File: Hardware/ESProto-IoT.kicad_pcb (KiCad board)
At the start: 2 copper layers, 68.6 x 53.3 mm, 55 parts, among them IC1 ARDUINO_PRO_MINI_5V, P1 DIGITAL_02, P10 DIGITAL_11, P11 DIGITAL_12, P12 DIGITAL_13X, P13 ANALOG_00, P14 ANALOG_01, P15 ANALOG_02, P16 ANALOG_03X, P17 I2C_01, P18 I2C_02, P19 I2C_03, P2 DIGITAL_03, P20 I2C_04, P21 POWER_L, P22 POWER_R, P23 ESP_G14, P24 ESP_G12, P25 ESP_G13, P26 ESP_3V3, P27 ESP_RST, P28 ESP_ADC, P29 ESP_G16, P3 DIGITAL_04, P30 LEVEL_T1, P31 LEVEL_B3, P32 ESP_TX, P33 ESP_RX, P34 ESP_G5, P35 ESP_G4, P36 LEVEL_B2, P37 LEVEL_B1, P38 ESP_G0, P39 ESP_G2, P4 DIGITAL_05, P40 ESP_G15, P41 ESP_GND, P42 ARDUINO_L, P43 I2C_A4_A5, P44 ARDUINO_R, P45 J_RAW_5V, P5 DIGITAL_06, P6 DIGITAL_07, P7 DIGITAL_08, P8 DIGITAL_09, P9 DIGITAL_10, SW1 PROGRAM

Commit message: Update to v20160308
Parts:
- removed P31: LEVEL_B3, Pin_Headers:Pin_Header_Straight_1x06
- removed P36: LEVEL_B2, Pin_Headers:Pin_Header_Straight_1x06
- removed P37: LEVEL_B1, Pin_Headers:Pin_Header_Straight_1x06
- P21: value POWER_L -> LEVEL_A; footprint Pin_Headers:Pin_Header_Straight_1x03 -> Pin_Headers:Pin_Header_Straight_1x04
- P22: value POWER_R -> POWER_A
- P30: value LEVEL_T1 -> LEVEL_B; footprint Pin_Headers:Pin_Header_Straight_1x06 -> Pin_Headers:Pin_Header_Straight_1x04
- moved P22 43.5 mm to (124.1, 56.4)
- moved P21 37.8 mm to (125.5, 89.9), turned to 180 degrees
- moved R1 22.5 mm to (106.8, 83.4)
- moved P30 8.64 mm to (113.3, 89.9), turned to 180 degrees
- moved P12 2.62 mm to (142.2, 89.5)
- moved P19 2.62 mm to (149.9, 89.5)
- moved P8 2.62 mm to (132.1, 89.5)
- moved P10 2.62 mm to (137.2, 89.5)
- moved P11 2.62 mm to (139.7, 89.5)
- moved P15 2.62 mm to (144.8, 89.5)
- moved P16 2.62 mm to (147.3, 89.5)
- moved P20 2.62 mm to (152.4, 89.5)
- moved P7 2.62 mm to (129.5, 89.5)
- moved P9 2.62 mm to (134.6, 89.5)
- moved SW1 1.99 mm to (99.8, 85.5)
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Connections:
- P10 pad 2: Net-(P10-Pad2) -> Net-(P1-Pad2)
- P11 pad 2: Net-(P10-Pad2) -> Net-(P1-Pad2)
- P12 pad 2: Net-(P10-Pad2) -> Net-(P1-Pad2)
- P15 pad 2: Net-(P10-Pad2) -> Net-(P1-Pad2)
- P16 pad 2: Net-(P10-Pad2) -> Net-(P1-Pad2)
- P19 pad 2: Net-(P10-Pad2) -> Net-(P1-Pad2)
- P20 pad 2: Net-(P10-Pad2) -> Net-(P1-Pad2)
- P21 pad 1: +3V3 -> GND
- P21 pad 2: Net-(P1-Pad2) -> SDA
- P21 pad 3: +5V -> SCL
- P22 pad 2: Net-(P10-Pad2) -> Net-(P1-Pad2)
- P30 pad 1: SDA -> GND
- P30 pad 2: Net-(P30-Pad2) -> SDA_ESP
- P30 pad 3: +5V -> SCL_ESP
- P30 pad 4: GND -> +3V3
- P7 pad 2: Net-(P10-Pad2) -> Net-(P1-Pad2)
- P8 pad 2: Net-(P10-Pad2) -> Net-(P1-Pad2)
- P9 pad 2: Net-(P10-Pad2) -> Net-(P1-Pad2)
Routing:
- net GND: track 239.6 -> 172.1 mm
- net GPIO0: track 65.4 -> 10.5 mm, vias 1 -> 0
- net D10: track 97.6 -> 52.9 mm, vias 1 -> 2
- net A2: track 64.5 -> 20.2 mm
- net A1: track 64.5 -> 24.6 mm, vias 2 -> 0
- net D7: track 60.1 -> 28.0 mm
- net Net-(P10-Pad2): track 28.4 -> 0.00 mm
- net RST2: track 47.1 -> 71.7 mm, vias 2 -> 1
- net SCL_ESP: track 65.2 -> 41.8 mm
- net Net-(P1-Pad2): track 29.1 -> 51.7 mm
- net GPIO15: track 62.5 -> 40.7 mm, vias 2 -> 0
- net A0: track 42.7 -> 21.0 mm, vias 1 -> 0
- net GPIO2: track 58.1 -> 39.1 mm
- net +5V: track 147.2 -> 139.8 mm, vias 1 -> 0
- net D3: track 29.2 -> 36.3 mm
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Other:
- outline, holes or cut-outs redrawn
- board text added: "Arduino Pro Mini"
- board text added: "ESP8266"
- board text added: "HOLD DURING POWER ON TO"
- board text added: "J1"
- board text added: "J2"
- board text added: "J3"
- board text added: "J4"
- board text added: "PROGRAM"
- board text added: "SCL"
- board text added: "SDA"
- board text added: "VCC"
- board text added: "VCC SELECT"
- board text added: "Version 20160308"
- board text removed: "ESP8266 (WiFi)"
- board text removed: "ESProto"
- board text removed: "HOLD DURING POWER ON TO PROGRAM"
- board text removed: "IoT"
- board text removed: "VCC SEL"

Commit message: Updated IoT
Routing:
- net GND: track 172.1 -> 225.8 mm, vias 0 -> 3
- net GPIO0: track 10.5 -> 61.5 mm, vias 0 -> 1
- net Net-(P1-Pad2): track 51.7 -> 94.8 mm, vias 0 -> 3
- net A2: track 20.2 -> 60.9 mm, vias 0 -> 2
- net A1: track 24.6 -> 61.2 mm, vias 0 -> 2
- net A0: track 21.0 -> 56.5 mm, vias 0 -> 2
- net +3V3: track 134.9 -> 101.9 mm, vias 1 -> 0
- net SDA: track 91.8 -> 105.9 mm
- net Net-(P44-Pad4): track 34.1 -> 35.6 mm
- net Net-(P44-Pad1): track 24.1 -> 24.9 mm
- net (no net): track 0.00 -> 0.51 mm
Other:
- board text added: "The ESProto IoT is an ESP8266 WiFi microcontroller that drives an Arduino Pro Mini. Extra ports, more compatibility with existing sensors."
- board text added: "Wovyn ESProto IoT"
- board text removed: "The ESProto IoT has an ESP8266 WiFi microcontroller that drives an Arduino Pro Mini, for extra ports and compatibility with existing sensors and hardware."

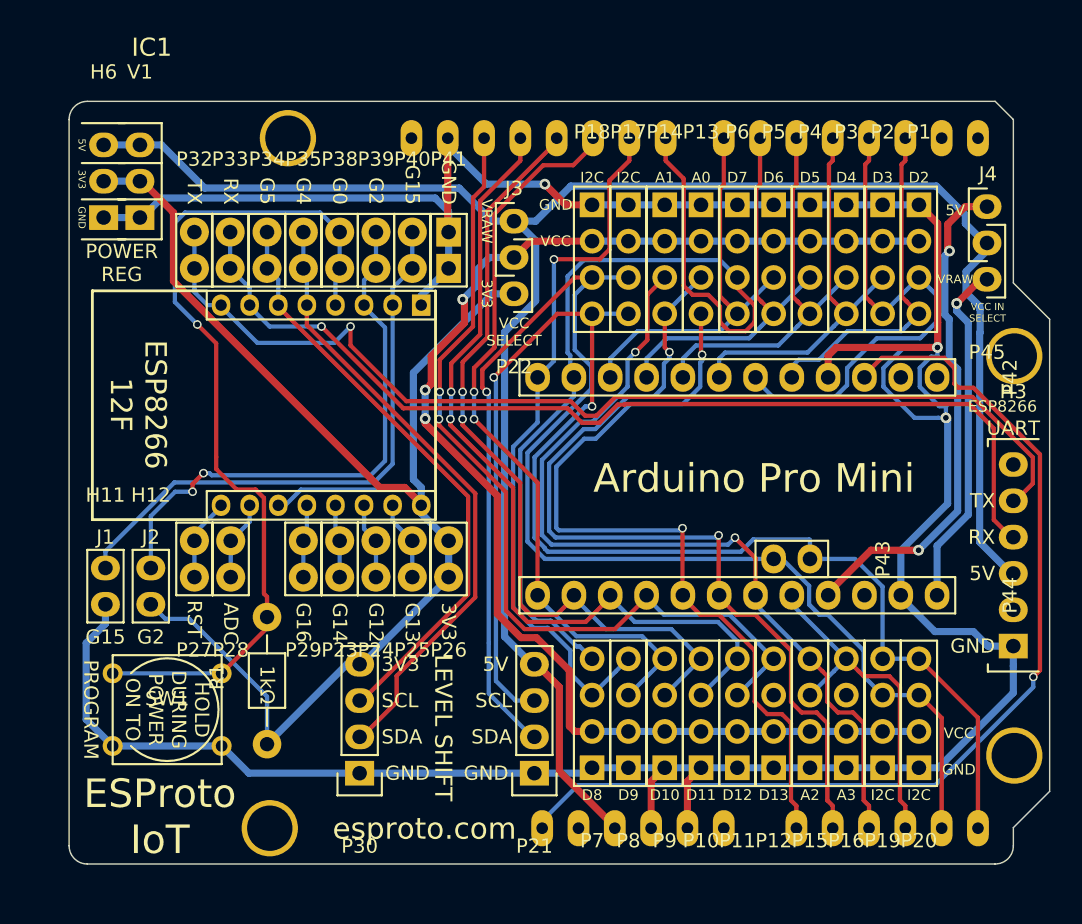
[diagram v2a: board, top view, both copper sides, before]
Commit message: Update to add more space, better labels
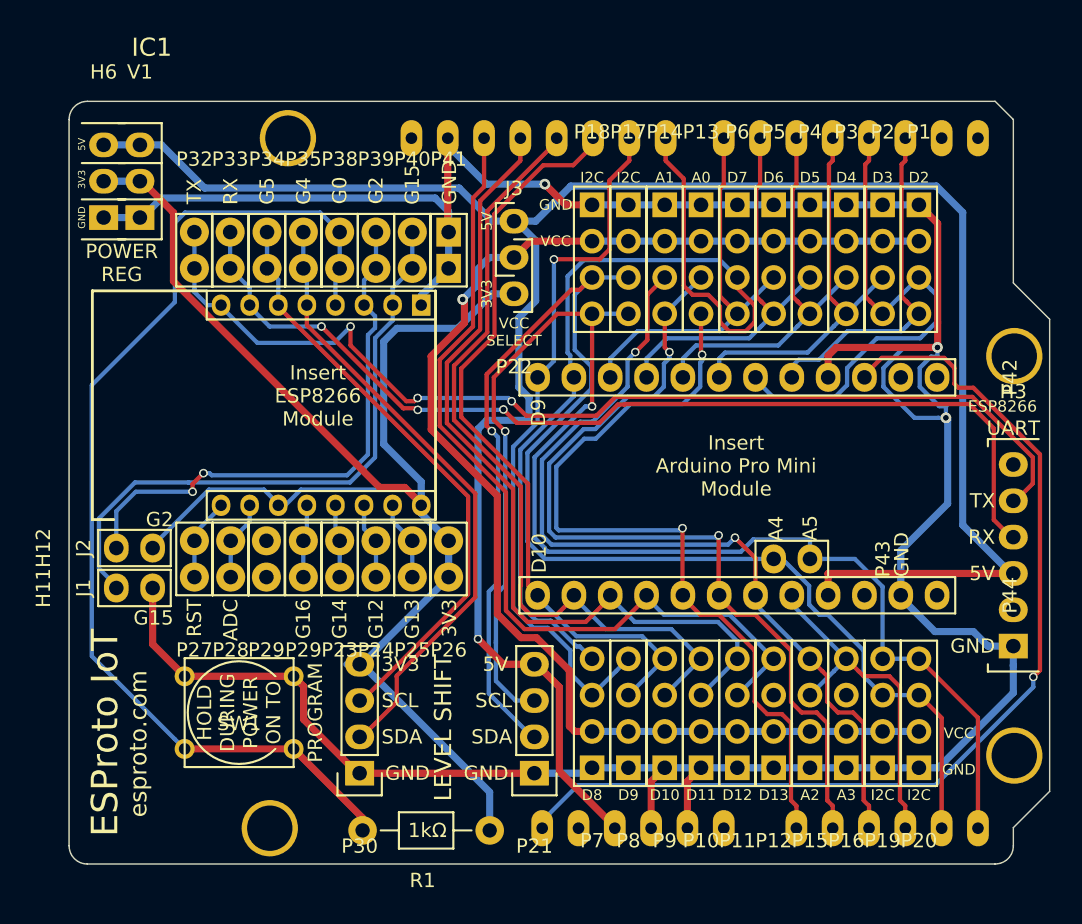
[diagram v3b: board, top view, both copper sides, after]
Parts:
- removed P45: J_RAW_5V, Pin_Headers:Pin_Header_Straight_1x03
- added P29: ESP_G16, Pin_Headers:Pin_Header_Straight_1x02, F.Cu at (106.8, 76.2)
- moved R1 15.3 mm to (117.9, 93.9), turned to 180 degrees
- moved SW1 5.04 mm to (104.9, 85.7), turned to 180 degrees
- moved H12 2.79 mm to (96.3, 74.2), turned to 90 degrees
- moved H11 1.59 mm to (96.3, 77.0), turned to 90 degrees
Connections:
- P44 pad 4: Net-(P44-Pad4) -> +5V
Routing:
- net Net-(P44-Pad4): track 35.6 -> 0.00 mm, vias 2 -> 0
- net Net-(P44-Pad1): track 24.9 -> 0.00 mm, vias 1 -> 0
- net +5V: track 139.8 -> 158.2 mm, vias 0 -> 1
- net GPIO0: track 61.5 -> 74.8 mm, vias 1 -> 0
- net +3V3: track 101.9 -> 110.5 mm
- net GND: track 225.8 -> 220.0 mm
- net GPIO15: track 40.7 -> 43.4 mm
- net D10: track 52.9 -> 53.6 mm, vias 2 -> 0
- net SCL: track 101.8 -> 102.6 mm
- net D11: track 56.1 -> 56.7 mm, vias 2 -> 0
- net (no net): track 0.51 -> 0.00 mm
- net Net-(P1-Pad2): track 94.8 -> 94.5 mm, vias 3 -> 1
- net D12: track 59.9 -> 60.1 mm, vias 2 -> 0
- net TXD1: track 74.3 -> 74.5 mm, vias 1 -> 3
- net D13: vias 2 -> 0
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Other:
- board text added: "A4"
- board text added: "A5"
- board text added: "Insert Arduino Pro Mini Module"
- board text added: "Insert ESP8266 Module"
- board text added: "Version 20160421"
- board text removed: "Arduino Pro Mini"
- board text removed: "ESP8266 12F"
- board text removed: "J4"
- board text removed: "VCC IN SELECT"
- board text removed: "VRAW"
- board text removed: "Version 20160308"
